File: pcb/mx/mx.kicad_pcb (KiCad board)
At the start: 2 copper layers, 133.3 x 113.3 mm, 68 parts, among them J4 Conn_01x06_Pin, J5 Conn_01x06_Pin, SW1 SW_PUSH, SW10 SW_PUSH, SW11 SW_PUSH, SW12 SW_PUSH, SW13 SW_PUSH, SW14 SW_PUSH, SW15 SW_PUSH, SW16 SW_PUSH, SW17 SW_PUSH, SW18 SW_PUSH, SW19 SW_PUSH, SW2 SW_PUSH, SW20 SW_PUSH, SW21 SW_PUSH, SW22 SW_PUSH, SW23 SW_PUSH, SW24 SW_PUSH, SW25 SW_PUSH, SW26 SW_PUSH, SW27 SW_PUSH, SW28 SW_PUSH, SW29 SW_PUSH, SW3 SW_PUSH, SW30 SW_PUSH, SW31 SW_PUSH, SW4 SW_PUSH, SW5 SW_PUSH, SW6 SW_PUSH, SW7 SW_PUSH, SW8 SW_PUSH, SW9 SW_PUSH

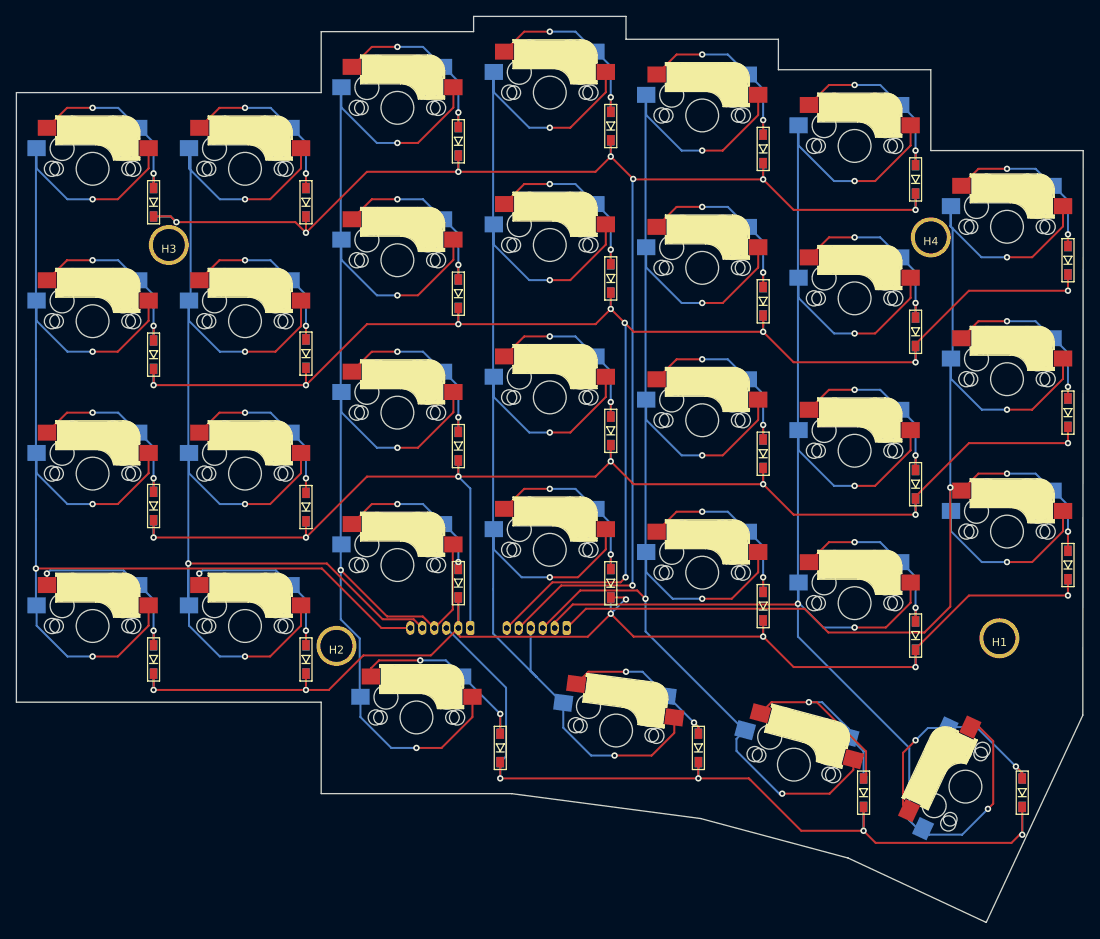
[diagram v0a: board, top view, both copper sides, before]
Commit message: Fix 穴の位置を微調整
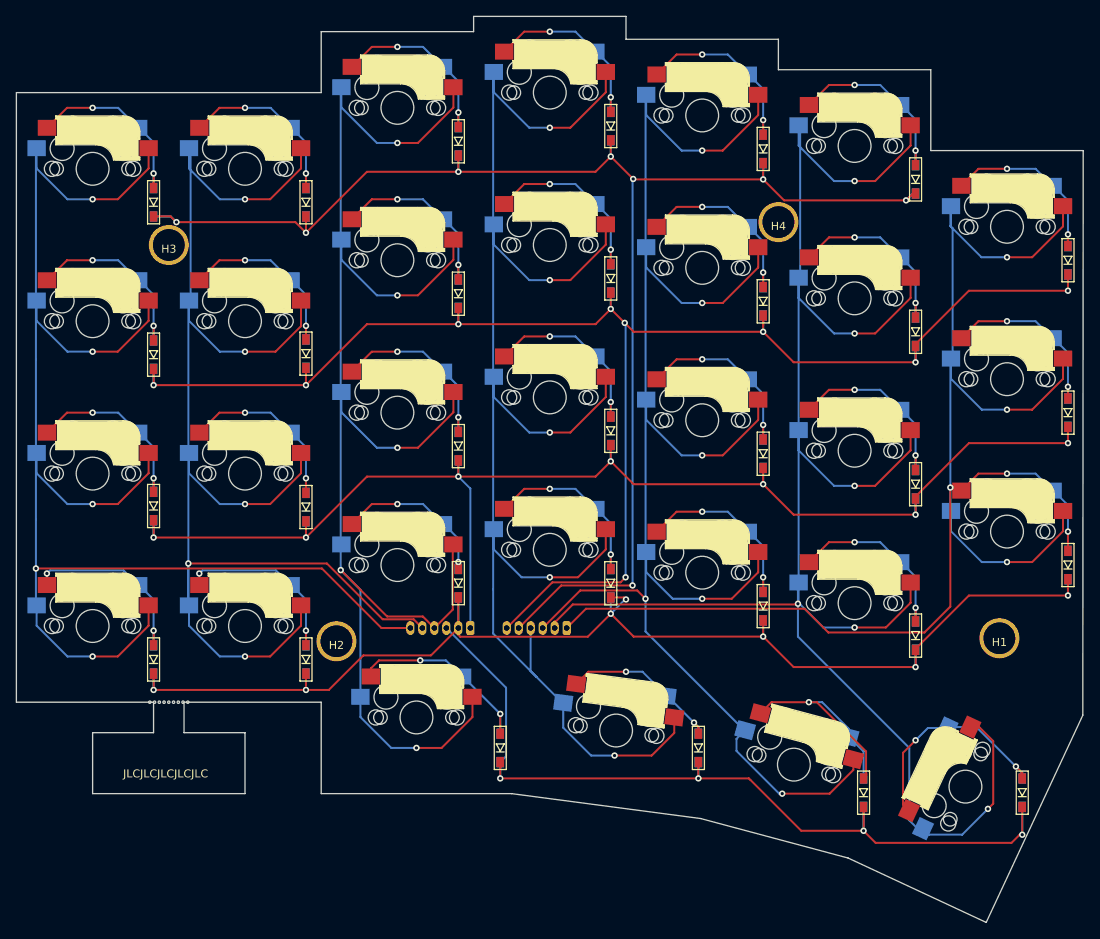
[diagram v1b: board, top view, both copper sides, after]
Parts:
- added REF**: Breakaway_Tabs, 0_kbd:Breakaway_Tabs, F.Cu at (75.3, 104.8)
- moved H4 19.1 mm to (151.5, 44.8)
- moved H2 0.58 mm to (96.2, 97.2)
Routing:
- net ROW0: track 193.6 -> 190.9 mm
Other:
- outline, holes or cut-outs redrawn
- board text added: "JLCJLCJLCJLCJLC"

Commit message: Fix 微調整
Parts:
- moved H1 14.2 mm to (166.7, 103.8)
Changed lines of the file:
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@@
     )
     (pad_to_mask_clearance 0)
-    (grid_origin 103.87 87.63)
+    (grid_origin 161.02 92.3925)
     (pcbplotparams
       (layerselection 0x00010fc_ffffffff)
@@
   )
   (footprint "0_kbd:M2_Hole_TH_Outside" (layer "F.Cu")
-    (at 179.1175 96.782573)
+    (at 166.735 103.8225)
     (property "Sheetfile" "mx.kicad_sch")
     (property "Sheetname" "")

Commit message: release: sage60 v0.0.1
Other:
- outline, holes or cut-outs redrawn
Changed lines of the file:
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@@
     )
     (pad_to_mask_clearance 0)
-    (grid_origin 161.02 92.3925)
+    (grid_origin 189.54624 102.403993)
     (pcbplotparams
       (layerselection 0x00010fc_ffffffff)
@@
     (pad "2" smd rect (at 5.7 -5.12 180) (size 2.3 2) (layers "B.Cu" "B.Paste" "B.Mask")
       (net 19 "Net-(D7-A)") (pinfunction "2") (pintype "passive"))
+    (model "C:/Projects/kbd/kicad-packages3D/kbd.3dshapes/kailh cherry socket soldered.step"
+      (offset (xyz -1 8 -3.7))
+      (scale (xyz 1 1 1))
+      (rotate (xyz 180 180 0))
+    )
   )
   (footprint "0_kbd:CherryMX_MidHeight_Hotswap" (layer "F.Cu")
@@
     (pad "2" smd rect (at 5.7 -5.12 180) (size 2.3 2) (layers "B.Cu" "B.Paste" "B.Mask")
       (net 20 "Net-(D8-A)") (pinfunction "2") (pintype "passive"))
+    (model "C:/Projects/kbd/kicad-packages3D/kbd.3dshapes/kailh cherry socket soldered.step"
+      (offset (xyz -1 8 -3.7))
+      (scale (xyz 1 1 1))
+      (rotate (xyz 180 180 0))
+    )
   )
   (footprint "0_kbd:CherryMX_MidHeight_Hotswap" (layer "F.Cu")
@@
     (pad "2" smd rect (at 5.7 -5.12 180) (size 2.3 2) (layers "B.Cu" "B.Paste" "B.Mask")
       (net 26 "Net-(D14-A)") (pinfunction "2") (pintype "passive"))
+    (model "C:/Projects/kbd/kicad-packages3D/kbd.3dshapes/kailh cherry socket soldered.step"
+      (offset (xyz 0 0 -3.5))
+      (scale (xyz 1 1 1))
+      (rotate (xyz 0 0 0))
+    )
   )
   (footprint "0_kbd:CherryMX_MidHeight_Hotswap" (layer "F.Cu")
@@
     (pad "2" smd rect (at 5.7 -5.12 180) (size 2.3 2) (layers "B.Cu" "B.Paste" "B.Mask")
       (net 27 "Net-(D15-A)") (pinfunction "2") (pintype "passive"))
+    (model "C:/Projects/kbd/kicad-packages3D/kbd.3dshapes/kailh cherry socket soldered.step"
+      (offset (xyz 0 0 -3.5))
+      (scale (xyz 1 1 1))
+      (rotate (xyz 0 0 0))
+    )
   )
   (footprint "0_kbd:M2_Hole_TH_Outside" (layer "F.Cu")
@@
   (gr_line (start 114.99 93.7015) (end 114.99 98.7015)
     (stroke (width 0.15) (type default)) (layer "Dwgs.User"))
-  (gr_line (start 189.54624 106.403993) (end 189.595 35.822573)
+  (gr_line (start 189.54624 102.403993) (end 182.9275 102.403993)
+    (stroke (width 0.1) (type default)) (layer "Edge.Cuts"))
+  (gr_line (start 189.595 92.972573) (end 189.595 35.822573)
     (stroke (width 0.1) (type default)) (layer "Edge.Cuts"))
   (gr_line (start 189.595 35.822573) (end 170.545 35.822573)
     (stroke (width 0.1) (type default)) (layer "Edge.Cuts"))
+  (gr_line (start 189.595 92.972573) (end 182.9275 92.972573)
+    (stroke (width 0.1) (type default)) (layer "Edge.Cuts"))
   (gr_line (start 177.469923 132.301738) (end 160.20476 124.250861)
     (stroke (width 0.1) (type default)) (layer "Edge.Cuts"))
@@
   (gr_line (start 132.445 19.05) (end 132.445 21.9075)
     (stroke (width 0.1) (type default)) (layer "Edge.Cuts"))
+  (gr_line (start 189.54624 106.403993) (end 189.54624 102.403993)
+    (stroke (width 0.1) (type default)) (layer "Edge.Cuts"))
   (gr_line (start 65.77 116.205) (end 65.77 108.585)
     (stroke (width 0.1) (type default)) (layer "Edge.Cuts"))
@@
   (gr_line (start 73.39 104.775) (end 56.245 104.775)
     (stroke (width 0.1) (type default)) (layer "Edge.Cuts"))
+  (gr_line (start 182.9275 92.972573) (end 182.9275 102.403993)
+    (stroke (width 0.1) (type default)) (layer "Edge.Cuts"))
   (gr_line (start 132.445 21.9075) (end 151.495 21.9075)
